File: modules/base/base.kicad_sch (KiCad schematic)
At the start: 26 parts

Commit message: Add power/gnd jacks
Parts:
- added J1: Power, BreadModular_AudioJacks:Jack_3.5mm_QingPu_WQP-PJ366ST_Vertical, symbol Connector_Audio:AudioJack3
- added J2: Ground, BreadModular_AudioJacks:Jack_3.5mm_QingPu_WQP-PJ366ST_Vertical, symbol Connector_Audio:AudioJack3
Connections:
- net +5V: now also J1.T
- net GND: now also J1.S, J2.S

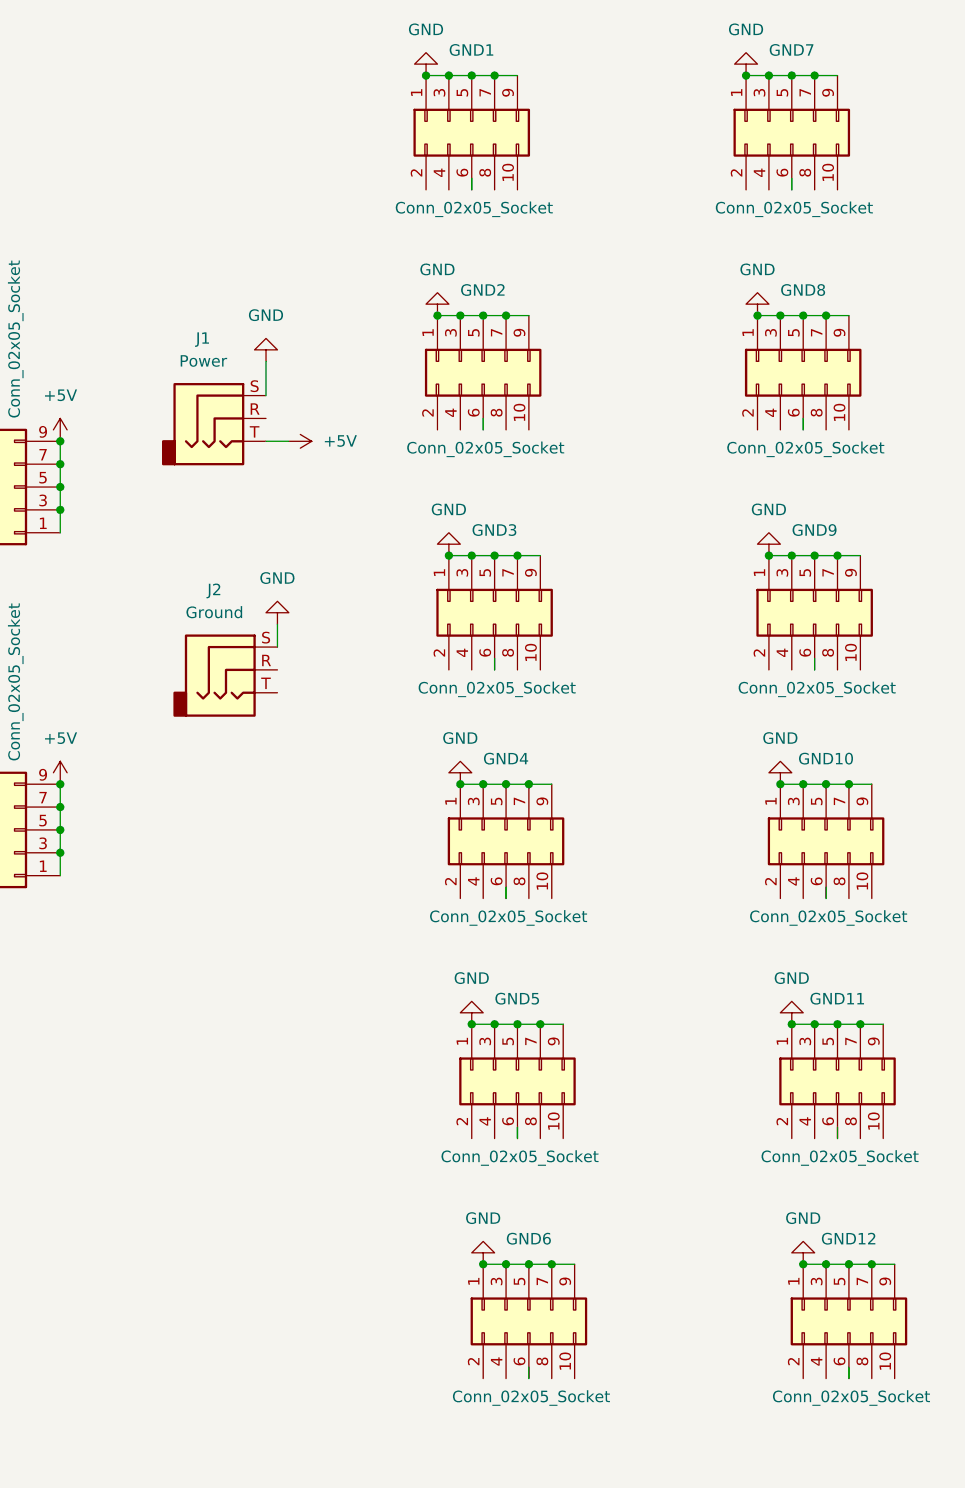
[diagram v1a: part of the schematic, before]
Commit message: Add 2 jack sockets for cascading support.
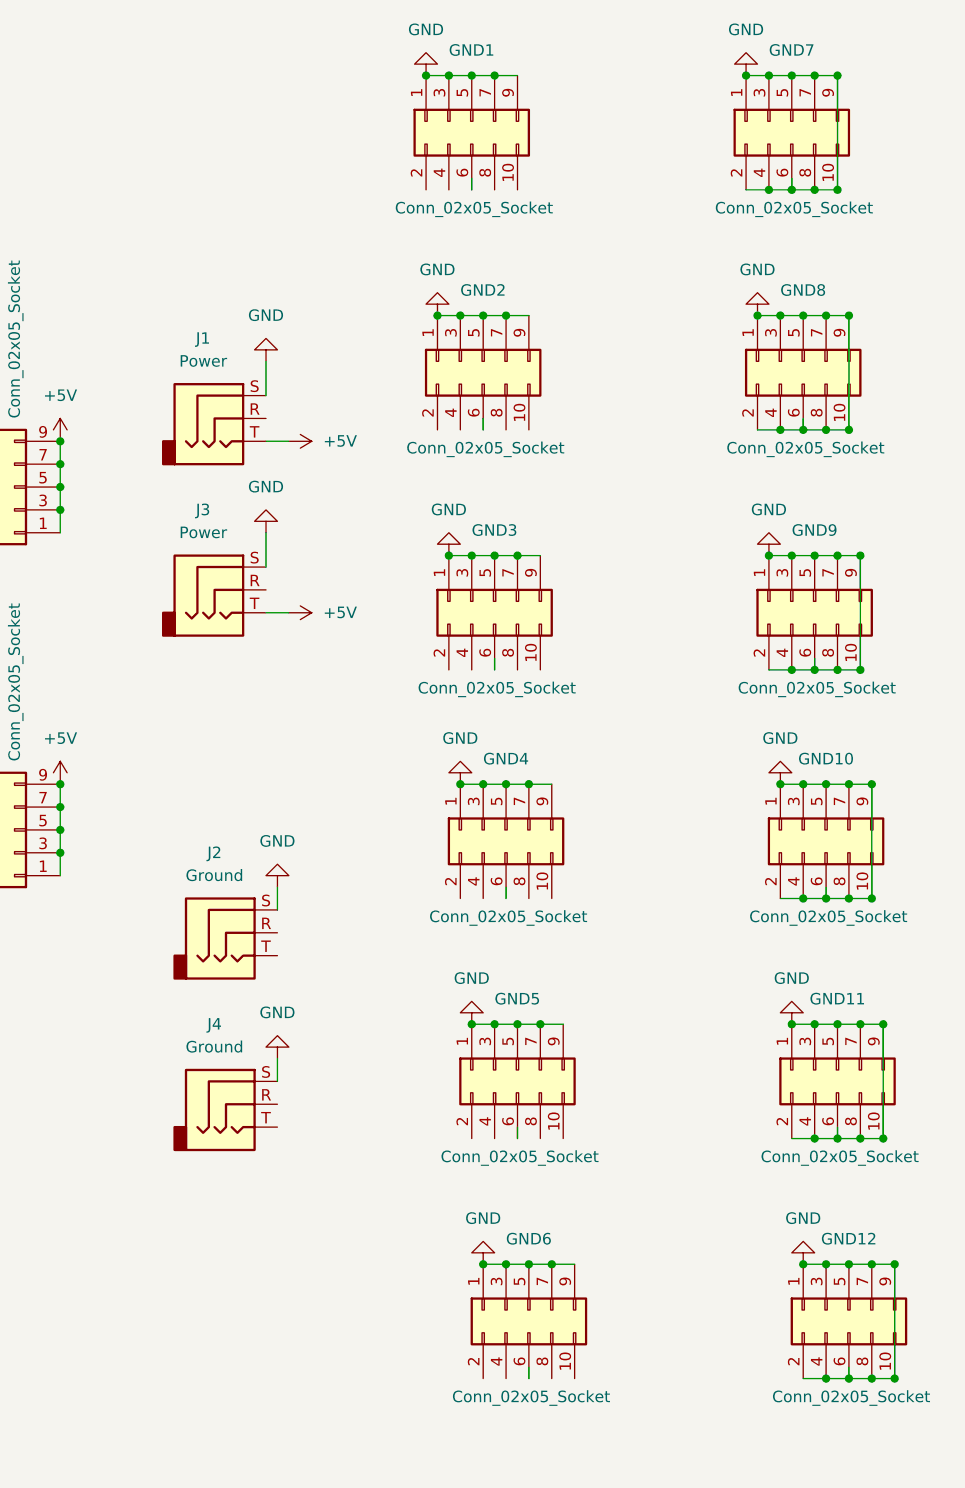
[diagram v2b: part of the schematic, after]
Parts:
- added J3: Power, BreadModular_AudioJacks:Jack_3.5mm_QingPu_WQP-PJ366ST_Vertical, symbol Connector_Audio:AudioJack3
- added J4: Ground, BreadModular_AudioJacks:Jack_3.5mm_QingPu_WQP-PJ366ST_Vertical, symbol Connector_Audio:AudioJack3
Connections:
- net +5V: now also J3.T
- net GND: now also GND10.10 (Pin_10), GND10.2 (Pin_2), GND10.4 (Pin_4), GND10.6 (Pin_6), GND10.8 (Pin_8), GND11.10 (Pin_10), GND11.2 (Pin_2), GND11.4 (Pin_4), GND11.6 (Pin_6), GND11.8 (Pin_8), GND12.10 (Pin_10), GND12.2 (Pin_2), GND12.4 (Pin_4), GND12.6 (Pin_6), GND12.8 (Pin_8), GND7.10 (Pin_10), GND7.2 (Pin_2), GND7.4 (Pin_4), GND7.6 (Pin_6), GND7.8 (Pin_8), GND8.10 (Pin_10), GND8.2 (Pin_2), GND8.4 (Pin_4), GND8.6 (Pin_6), GND8.8 (Pin_8), GND9.10 (Pin_10), GND9.2 (Pin_2), GND9.4 (Pin_4), GND9.6 (Pin_6), GND9.8 (Pin_8), J3.S, J4.S
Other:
- moved on the sheet: J2

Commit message: base: Add USB power setup to the base
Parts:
- added C1, C6: 100uf, Capacitor_SMD:C_1206_3216Metric, symbol Device:C
- added C2, C4: 0.1uf, Capacitor_SMD:C_0805_2012Metric, symbol Device:C
- added C5: 10nf, Capacitor_SMD:C_0805_2012Metric, symbol Device:C
- added D1: LED, LED_SMD:LED_0603_1608Metric, symbol Device:LED
- added FB1, FB2: GZ2012E800TF, Capacitor_SMD:C_0805_2012Metric, symbol Device:FerriteBead_Small
- added J5: USB_C_Receptacle_PowerOnly_6P, BreadModular_TypeC:HRO-TYPE-C-31-M-12, symbol Connector:USB_C_Receptacle_PowerOnly_6P
- added R1: 1k, Resistor_SMD:R_0402_1005Metric, symbol Device:R
- added R2, R3: 5.1k, Resistor_SMD:R_0603_1608Metric, symbol Device:R
- added U1: AMS1117-3.3, Package_TO_SOT_SMD:SOT-223, symbol Regulator_Linear:AMS1117-3.3
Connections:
- net +5V: now also C1.1, C2.1, FB1.1, J5.A9 (VBUS), J5.B9 (VBUS); no longer 5V1.10 (Pin_10), 5V1.2 (Pin_2), 5V1.4 (Pin_4), 5V1.6 (Pin_6), 5V1.8 (Pin_8), 5V11.10 (Pin_10), 5V11.2 (Pin_2), 5V11.4 (Pin_4), 5V11.6 (Pin_6), 5V11.8 (Pin_8), 5V12.10 (Pin_10), 5V12.2 (Pin_2), 5V12.4 (Pin_4), 5V12.6 (Pin_6), 5V12.8 (Pin_8), 5V13.1 (Pin_1), 5V13.3 (Pin_3), 5V13.5 (Pin_5), 5V13.7 (Pin_7), 5V13.9 (Pin_9), 5V14.1 (Pin_1), 5V14.3 (Pin_3), 5V14.5 (Pin_5), 5V14.7 (Pin_7), 5V14.9 (Pin_9), 5V2.10 (Pin_10), 5V2.2 (Pin_2), 5V2.4 (Pin_4), 5V2.6 (Pin_6), 5V2.8 (Pin_8), 5V3.10 (Pin_10), 5V3.2 (Pin_2), 5V3.4 (Pin_4), 5V3.6 (Pin_6), 5V3.8 (Pin_8), 5V5.10 (Pin_10), 5V5.2 (Pin_2), 5V5.4 (Pin_4), 5V5.6 (Pin_6), 5V5.8 (Pin_8), 5V6.10 (Pin_10), 5V6.2 (Pin_2), 5V6.4 (Pin_4), 5V6.6 (Pin_6), 5V6.8 (Pin_8), 5V7.10 (Pin_10), 5V7.2 (Pin_2), 5V7.4 (Pin_4), 5V7.6 (Pin_6), 5V7.8 (Pin_8), 5V8.10 (Pin_10), 5V8.2 (Pin_2), 5V8.4 (Pin_4), 5V8.6 (Pin_6), 5V8.8 (Pin_8), 5V9.10 (Pin_10), 5V9.2 (Pin_2), 5V9.4 (Pin_4), 5V9.6 (Pin_6), 5V9.8 (Pin_8)
- net GND: now also C1.2, C2.2, C4.2, C5.2, C6.2, J5.A12 (GND), J5.B12 (GND), R1.2, R2.2, R3.2, U1.1 (GND)
- new net: J5.A5 (CC1), R3.1
- new net: FB2.1, U1.2 (VO)
- new net: FB1.2, U1.3 (VI)
- new net: J5.B5 (CC2), R2.1
- new net: C5.1, J5.S1 (SHIELD)
- new net: D1.1 (K), R1.1
- new net +3.3V: 5V1.10 (Pin_10), 5V1.2 (Pin_2), 5V1.4 (Pin_4), 5V1.6 (Pin_6), 5V1.8 (Pin_8), 5V11.10 (Pin_10), 5V11.2 (Pin_2), 5V11.4 (Pin_4), 5V11.6 (Pin_6), 5V11.8 (Pin_8), 5V12.10 (Pin_10), 5V12.2 (Pin_2), 5V12.4 (Pin_4), 5V12.6 (Pin_6), 5V12.8 (Pin_8), 5V13.1 (Pin_1), 5V13.3 (Pin_3), 5V13.5 (Pin_5), 5V13.7 (Pin_7), 5V13.9 (Pin_9), 5V14.1 (Pin_1), 5V14.3 (Pin_3), 5V14.5 (Pin_5), 5V14.7 (Pin_7), 5V14.9 (Pin_9), 5V2.10 (Pin_10), 5V2.2 (Pin_2), 5V2.4 (Pin_4), 5V2.6 (Pin_6), 5V2.8 (Pin_8), 5V3.10 (Pin_10), 5V3.2 (Pin_2), 5V3.4 (Pin_4), 5V3.6 (Pin_6), 5V3.8 (Pin_8), 5V5.10 (Pin_10), 5V5.2 (Pin_2), 5V5.4 (Pin_4), 5V5.6 (Pin_6), 5V5.8 (Pin_8), 5V6.10 (Pin_10), 5V6.2 (Pin_2), 5V6.4 (Pin_4), 5V6.6 (Pin_6), 5V6.8 (Pin_8), 5V7.10 (Pin_10), 5V7.2 (Pin_2), 5V7.4 (Pin_4), 5V7.6 (Pin_6), 5V7.8 (Pin_8), 5V8.10 (Pin_10), 5V8.2 (Pin_2), 5V8.4 (Pin_4), 5V8.6 (Pin_6), 5V8.8 (Pin_8), 5V9.10 (Pin_10), 5V9.2 (Pin_2), 5V9.4 (Pin_4), 5V9.6 (Pin_6), 5V9.8 (Pin_8), C4.1, C6.1, D1.2 (A), FB2.2

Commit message: base: Remove power extention via TRS cable Even with the regulator, it's noisy. So, instead now we use TRS only for syncing the ground between boards
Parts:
- J1, J3: value Power -> Ground
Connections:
- net +5V: no longer J1.T, J3.T
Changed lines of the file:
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@@
 	(wire
 		(pts
-			(xy 184.15 86.36) (xy 181.61 86.36)
-		)
-		(stroke
-			(width 0)
-			(type default)
-		)
-	)
-	(wire
-		(pts
 			(xy 146.05 110.49) (xy 146.05 113.03)
 		)
@@
 	(wire
 		(pts
-			(xy 184.15 67.31) (xy 181.61 67.31)
-		)
-		(stroke
-			(width 0)
-			(type default)
-		)
-	)
-	(wire
-		(pts
 			(xy 33.02 259.08) (xy 46.99 259.08)
 		)
@@
 			)
 		)
-		(property "Value" "Power"
+		(property "Value" "Ground"
 			(at 174.625 58.42 0)
 			(effects
@@
 	)
 	(symbol
-		(lib_id "power:+5V")
-		(at 184.15 86.36 270)
-		(unit 1)
-		(exclude_from_sim no)
-		(in_bom yes)
-		(on_board yes)
-		(dnp no)
-		(fields_autoplaced yes)
-		(property "Reference" "#PWR033"
-			(at 180.34 86.36 0)
-			(effects
-				(font
-					(size 1.27 1.27)
-				)
-				(hide yes)
-			)
-		)
-		(property "Value" "+5V"
-			(at 187.96 86.3599 90)
-			(effects
-				(font
-					(size 1.27 1.27)
-				)
-				(justify left)
-			)
-		)
-		(property "Footprint" ""
-			(at 184.15 86.36 0)
-			(effects
-				(font
-					(size 1.27 1.27)
-				)
-				(hide yes)
-			)
-		)
-		(property "Datasheet" ""
-			(at 184.15 86.36 0)
-			(effects
-				(font
-					(size 1.27 1.27)
-				)
-				(hide yes)
-			)
-		)
-		(property "Description" "Power symbol creates a global label with name \"+5V\""
-			(at 184.15 86.36 0)
-			(effects
-				(font
-					(size 1.27 1.27)
-				)
-				(hide yes)
-			)
-		)
-		(pin "1"
-		)
-		(instances
-			(project "base"
-				(path "/b63493d3-5f6d-47e3-845b-87e7090fc1ab"
-					(reference "#PWR033")
-					(unit 1)
-				)
-			)
-		)
-	)
-	(symbol
 		(lib_id "power:GND")
 		(at 201.93 80.01 180)
@@
 			)
 		)
-		(property "Value" "Power"
+		(property "Value" "Ground"
 			(at 174.625 77.47 0)
 			(effects
@@
 					(unit 1)
 				)
-			)
-		)
-	)
-	(symbol
-		(lib_id "power:+5V")
-		(at 184.15 67.31 270)
-		(unit 1)
-		(exclude_from_sim no)
-		(in_bom yes)
-		(on_board yes)
-		(dnp no)
-		(fields_autoplaced yes)
-		(property "Reference" "#PWR031"
-			(at 180.34 67.31 0)
-			(effects
-				(font
-					(size 1.27 1.27)
-				)
-				(hide yes)
-			)
-		)
-		(property "Value" "+5V"
-			(at 187.96 67.3099 90)
-			(effects
-				(font
-					(size 1.27 1.27)
-				)
-				(justify left)
-			)
-		)
-		(property "Footprint" ""
-			(at 184.15 67.31 0)
-			(effects
-				(font
-					(size 1.27 1.27)
-				)
-				(hide yes)
-			)
-		)
-		(property "Datasheet" ""
-			(at 184.15 67.31 0)
-			(effects
-				(font
-					(size 1.27 1.27)
-				)
-				(hide yes)
-			)
-		)
-		(property "Description" "Power symbol creates a global label with name \"+5V\""
-			(at 184.15 67.31 0)
-			(effects
-				(font
-					(size 1.27 1.27)
-				)
-				(hide yes)
-			)
-		)
-		(pin "1"
-		)
-		(instances
-			(project "base"
-				(path "/b63493d3-5f6d-47e3-845b-87e7090fc1ab"
-					(reference "#PWR031")
-					(unit 1)
-				)
